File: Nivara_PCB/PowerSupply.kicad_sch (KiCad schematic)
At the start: 16 parts, among them U2 AP63203WU, U3 AP63205WU

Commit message: Cambios en el RS485
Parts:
- renumbered TP4 to TP2, TP2 to TP3, TP3 to TP4
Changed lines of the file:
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@@
 		(on_board yes)
 		(dnp no)
-		(property "Reference" "TP4"
+		(property "Reference" "TP2"
 			(at 91.186 57.912 0)
 			(effects
@@
 			(project "Nivara_PCB"
 				(path "/13184db0-a71d-4054-b13a-bbf46d2b100d/4e7fa7f2-8bf5-4f9c-874d-fa1b4fd76f92/c8cd749e-9134-4d76-b8ef-ce0eb3eb606f"
-					(reference "TP4")
+					(reference "TP2")
 					(unit 1)
 				)
@@
 		(on_board yes)
 		(dnp no)
-		(property "Reference" "TP3"
+		(property "Reference" "TP4"
 			(at 112.776 93.472 0)
 			(effects
@@
 			(project "Nivara_PCB"
 				(path "/13184db0-a71d-4054-b13a-bbf46d2b100d/4e7fa7f2-8bf5-4f9c-874d-fa1b4fd76f92/c8cd749e-9134-4d76-b8ef-ce0eb3eb606f"
-					(reference "TP3")
+					(reference "TP4")
 					(unit 1)
 				)
@@
 		(dnp no)
 		(fields_autoplaced yes)
-		(property "Reference" "#PWR015"
+		(property "Reference" "#PWR021"
 			(at 71.12 123.19 0)
 			(effects
@@
 			(project "Nivara_PCB"
 				(path "/13184db0-a71d-4054-b13a-bbf46d2b100d/4e7fa7f2-8bf5-4f9c-874d-fa1b4fd76f92/c8cd749e-9134-4d76-b8ef-ce0eb3eb606f"
-					(reference "#PWR015")
+					(reference "#PWR021")
 					(unit 1)
 				)
@@
 		(on_board yes)
 		(dnp no)
-		(property "Reference" "TP2"
+		(property "Reference" "TP3"
 			(at 112.776 45.212 0)
 			(effects
@@
 			(project "Nivara_PCB"
 				(path "/13184db0-a71d-4054-b13a-bbf46d2b100d/4e7fa7f2-8bf5-4f9c-874d-fa1b4fd76f92/c8cd749e-9134-4d76-b8ef-ce0eb3eb606f"
-					(reference "TP2")
+					(reference "TP3")
 					(unit 1)
 				)
@@
 		(dnp no)
 		(fields_autoplaced yes)
-		(property "Reference" "#PWR014"
+		(property "Reference" "#PWR020"
 			(at 71.12 73.66 0)
 			(effects
@@
 			(project ""
 				(path "/13184db0-a71d-4054-b13a-bbf46d2b100d/4e7fa7f2-8bf5-4f9c-874d-fa1b4fd76f92/c8cd749e-9134-4d76-b8ef-ce0eb3eb606f"
-					(reference "#PWR014")
-					(unit 1)
-				)
+					(reference "#PWR020")
+					(unit 1)
+				)

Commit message: Cambios en la power supply.
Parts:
- removed C3: 10uF, PCM_Capacitor_SMD_AKL:C_1206_3216Metric, symbol PCM_Capacitor_AKL:C_1206
- removed C6, C8, C9: 22uF, PCM_Capacitor_SMD_AKL:C_0805_2012Metric, symbol PCM_Capacitor_AKL:C_0805
- removed L1, L2: 4u7H, Inductor_SMD:L_APV_ANR6028, symbol Device:L_Iron
- removed U2: AP63203WU, Package_TO_SOT_SMD:TSOT-23-6, symbol Regulator_Switching:AP63203WU
- removed U3: AP63205WU, Package_TO_SOT_SMD:TSOT-23-6, symbol Regulator_Switching:AP63205WU
- added C11: 100pF, PCM_Capacitor_SMD_AKL:C_0805_2012Metric, symbol PCM_Capacitor_AKL:C_0805
- added C12, C3, C8, C9: 22uF, PCM_Capacitor_SMD_AKL:C_0603_1608Metric, symbol PCM_Capacitor_AKL:C_0603
- added C13: 10uF, PCM_Capacitor_SMD_AKL:C_1206_3216Metric, symbol PCM_Capacitor_AKL:C_1206
- added JP1, JP2: SolderJumper_2_Open, Jumper:SolderJumper-2_P1.3mm_Open_Pad1.0x1.5mm, symbol Jumper:SolderJumper_2_Open
- added L1, L3: CXP0420-6R8M-AG(6.8UH), Fuse_Holder:IND-SMD_L4.4-W4.2_CXP0420, symbol Fuse_Holder:CXP0420-6R8M-AG(6.8UH)
- added R31: 196k, PCM_Resistor_SMD_AKL:R_0603_1608Metric, symbol PCM_Resistor_US_AKL:R_0603
- added R32: 62k, PCM_Resistor_SMD_AKL:R_0603_1608Metric, symbol PCM_Resistor_US_AKL:R_0603
- added R33: 157k, PCM_Resistor_SMD_AKL:R_0603_1608Metric, symbol PCM_Resistor_US_AKL:R_0603
- added R34: 30k, PCM_Resistor_SMD_AKL:R_0603_1608Metric, symbol PCM_Resistor_US_AKL:R_0603
- added TP5: +5Vout, TestPoint:TestPoint_Pad_1.0x1.0mm, symbol Connector:TestPoint_Probe
- added TP6: +5V, TestPoint:TestPoint_Pad_1.0x1.0mm, symbol Connector:TestPoint_Probe
- added TP7: +3.3Vout, TestPoint:TestPoint_Pad_1.0x1.0mm, symbol Connector:TestPoint_Probe
- added TP8: FB, TestPoint:TestPoint_Pad_1.0x1.0mm, symbol Connector:TestPoint_Probe
- added U2, U7: AP63200WU, Package_TO_SOT_SMD:TSOT-23-6, symbol Regulator_Switching:AP63200WU
- C2: Voltaje (none) -> 50V
- C7: value 22uF -> 100pF
- TP4: value +5V -> FB
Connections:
- net +3.3V: now also JP1.2 (B), JP2.2 (B), TP5.1, TP7.1; no longer TP3.1
- net GND: now also C12.2, C13.2, C3.2, C8.2, C9.2, R32.2, R34.2, U2.4 (GND), U7.4 (GND); no longer C7.2
- net VCC: now also C13.1, U2.2 (EN), U2.3 (IN), U7.2 (EN), U7.3 (IN)
- net at C5.2: now also L1.1, U2.5 (SW)
- net at C4.2: now also L3.1, U7.5 (SW)
- net at C4.1: now also U7.6 (BST)
- net at C5.1: now also U2.6 (BST)
- net +5V: no longer names the net of TP4.1
- net +5V: now also C11.1, R31.2, R32.1, U7.1 (FB); no longer C7.1
- new net: C7.2, C8.1, C9.1, JP2.1 (A), L1.2, R33.1, TP6.1
- new net: C11.2, C12.1, C3.1, JP1.1 (A), L3.2, R31.1, TP3.1
- new net: C7.1, R33.2, R34.1, TP8.1, U2.1 (FB)
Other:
- note added: "Regulador a 5V"
- note removed: "Regulador a 12V"
- moved on the sheet: TP2, TP3

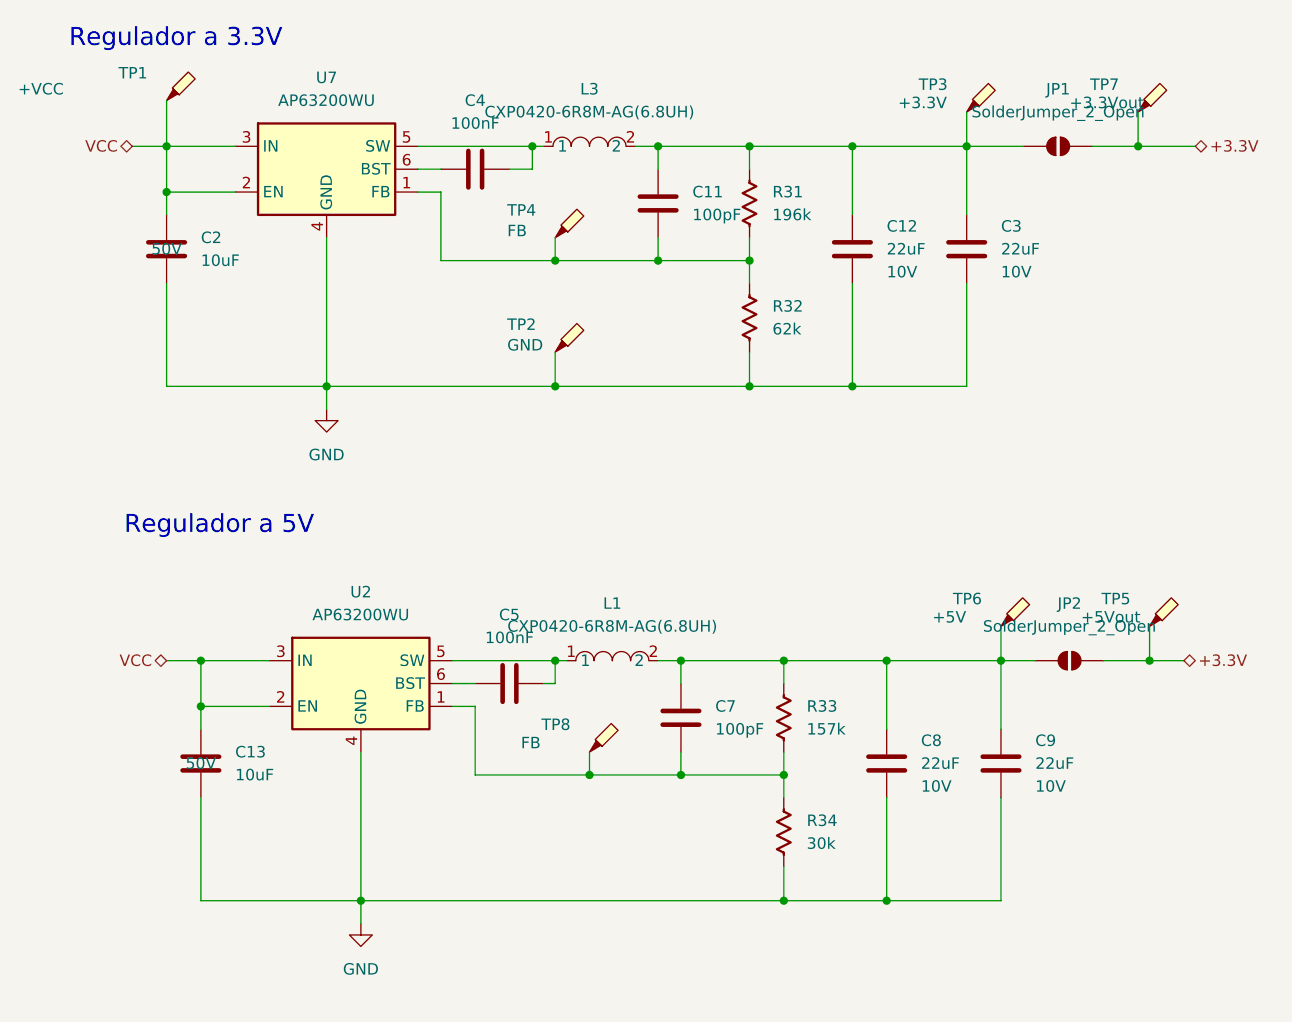
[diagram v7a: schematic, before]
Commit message: Cambio de IntelliFet, porque los que tenían no estaban disponibles.
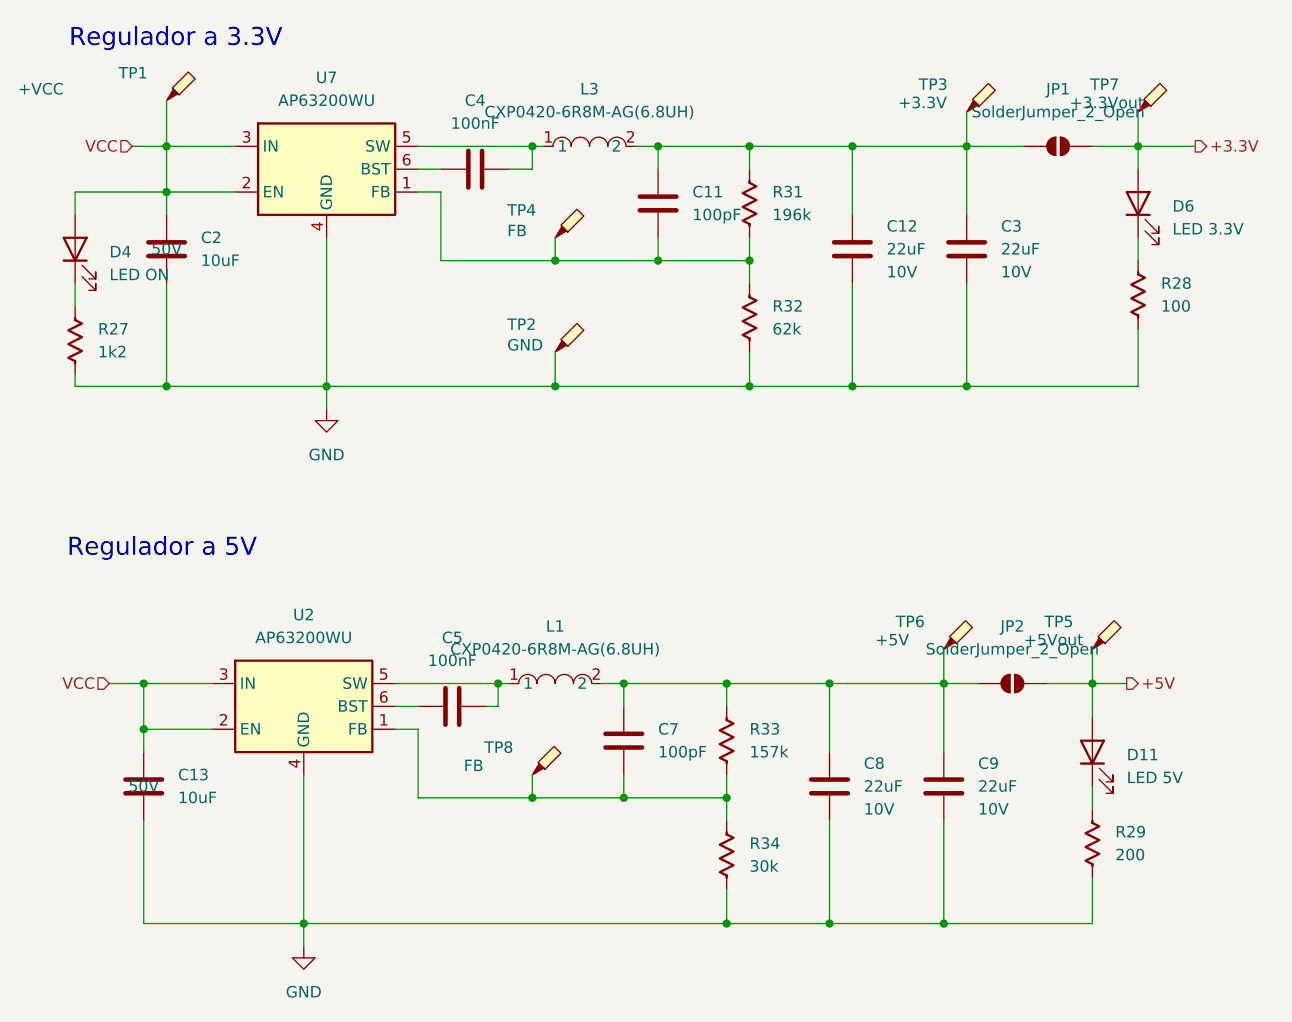
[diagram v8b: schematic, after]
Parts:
- added D11: LED 5V, LED_SMD:LED_0603_1608Metric, symbol Device:LED
- added D4: LED ON, LED_SMD:LED_0603_1608Metric, symbol Device:LED
- added D6: LED 3.3V, LED_SMD:LED_0603_1608Metric, symbol Device:LED
- added R27: 1k2, PCM_Resistor_SMD_AKL:R_0603_1608Metric, symbol PCM_Resistor_US_AKL:R_0603
- added R28: 100, PCM_Resistor_SMD_AKL:R_0603_1608Metric, symbol PCM_Resistor_US_AKL:R_0603
- added R29: 200, PCM_Resistor_SMD_AKL:R_0603_1608Metric, symbol PCM_Resistor_US_AKL:R_0603
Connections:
- net +3.3V: now also D6.2 (A); no longer JP2.2 (B), TP5.1
- net GND: now also R27.1, R28.1, R29.1
- net VCC: now also D4.2 (A)
- new net: D6.1 (K), R28.2
- new net: D11.1 (K), R29.2
- new net: D4.1 (K), R27.2
- new net +5V: D11.2 (A), JP2.2 (B), TP5.1
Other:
- moved on the sheet: C13, C5, C7, C8, C9, JP2, L1, R33, R34, TP5, TP6, TP8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
